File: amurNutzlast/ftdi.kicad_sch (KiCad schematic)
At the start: 23 parts, among them U4 FT2232HL, U5 93LCxxA, Y1 Crystal_GND24_Small

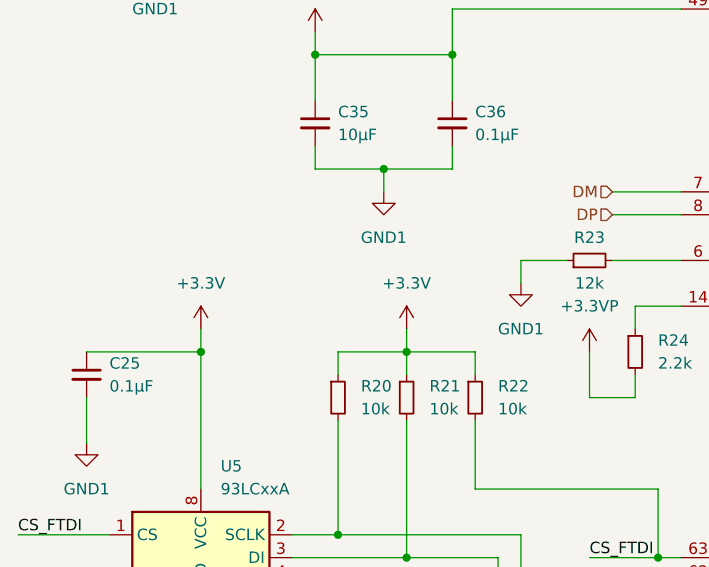
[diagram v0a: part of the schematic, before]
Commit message: ftdi layout finish
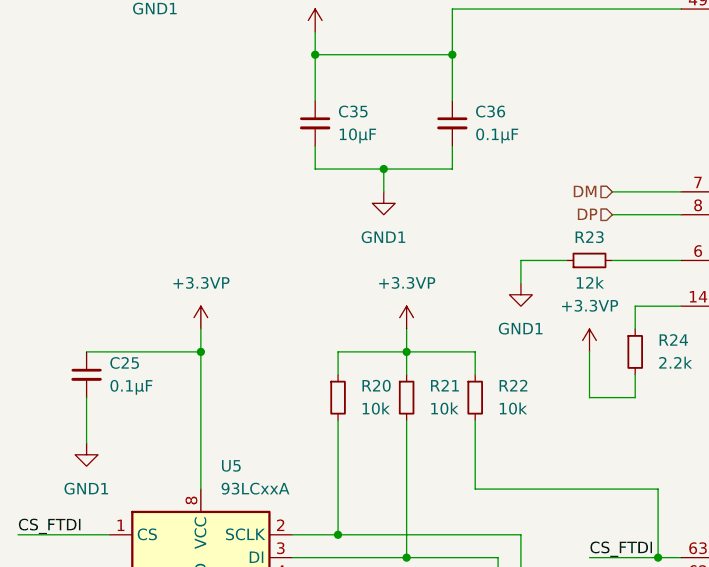
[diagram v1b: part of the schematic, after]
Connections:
- net +3.3V is gone; now on net +3.3VP: C25.1, R20.1, R21.1, R22.1, U5.8 (VCC)
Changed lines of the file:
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@@
     (effects (font (size 1.27 1.27)) (justify left))
   )
-  (symbol (lib_id "power:+3.3V") (at 76.2 114.3 0) (unit 1)
-    (in_bom yes) (on_board yes) (dnp no) (fields_autoplaced)
-    (property "Reference" "#PWR057" (at 76.2 118.11 0)
-      (effects (font (size 1.27 1.27)) hide)
-    )
-    (property "Value" "+3.3V" (at 76.2 109.22 0)
-      (effects (font (size 1.27 1.27)))
-    )
-    (property "Footprint" "" (at 76.2 114.3 0)
-      (effects (font (size 1.27 1.27)) hide)
-    )
-    (property "Datasheet" "" (at 76.2 114.3 0)
-      (effects (font (size 1.27 1.27)) hide)
-    )
-    (pin "1")
-    (instances
-      (project "amurNutzlast"
-        (path "/81bb76b1-eb1b-4eda-9d04-3f9c2ab6907c/baccd8b0-0f8a-4d7f-90a2-78ebcab7896d"
-          (reference "#PWR057") (unit 1)
+  (symbol (lib_id "power:+3.3VP") (at 53.34 114.3 0) (unit 1)
+    (in_bom yes) (on_board yes) (dnp no) (fields_autoplaced)
+    (property "Reference" "#PWR055" (at 57.15 115.57 0)
+      (effects (font (size 1.27 1.27)) hide)
+    )
+    (property "Value" "+3.3VP" (at 53.34 109.22 0)
+      (effects (font (size 1.27 1.27)))
+    )
+    (property "Footprint" "" (at 53.34 114.3 0)
+      (effects (font (size 1.27 1.27)) hide)
+    )
+    (property "Datasheet" "" (at 53.34 114.3 0)
+      (effects (font (size 1.27 1.27)) hide)
+    )
+    (pin "1")
+    (instances
+      (project "amurNutzlast"
+        (path "/81bb76b1-eb1b-4eda-9d04-3f9c2ab6907c/baccd8b0-0f8a-4d7f-90a2-78ebcab7896d"
+          (reference "#PWR055") (unit 1)
         )
       )
@@
     )
   )
-  (symbol (lib_id "power:+3.3V") (at 53.34 114.3 0) (unit 1)
-    (in_bom yes) (on_board yes) (dnp no) (fields_autoplaced)
-    (property "Reference" "#PWR055" (at 53.34 118.11 0)
-      (effects (font (size 1.27 1.27)) hide)
-    )
-    (property "Value" "+3.3V" (at 53.34 109.22 0)
-      (effects (font (size 1.27 1.27)))
-    )
-    (property "Footprint" "" (at 53.34 114.3 0)
-      (effects (font (size 1.27 1.27)) hide)
-    )
-    (property "Datasheet" "" (at 53.34 114.3 0)
-      (effects (font (size 1.27 1.27)) hide)
-    )
-    (pin "1")
-    (instances
-      (project "amurNutzlast"
-        (path "/81bb76b1-eb1b-4eda-9d04-3f9c2ab6907c/baccd8b0-0f8a-4d7f-90a2-78ebcab7896d"
-          (reference "#PWR055") (unit 1)
-        )
-      )
-    )
-  )
   (symbol (lib_id "Device:Crystal_GND24_Small") (at 88.9 157.48 270) (unit 1)
     (in_bom yes) (on_board yes) (dnp no) (fields_autoplaced)
@@
         )
       )
+    )
+  )
+  (symbol (lib_id "power:+3.3VP") (at 76.2 114.3 0) (unit 1)
+    (in_bom yes) (on_board yes) (dnp no) (fields_autoplaced)
+    (property "Reference" "#PWR057" (at 80.01 115.57 0)
+      (effects (font (size 1.27 1.27)) hide)
+    )
+    (property "Value" "+3.3VP" (at 76.2 109.22 0)
+      (effects (font (size 1.27 1.27)))
+    )
+    (property "Footprint" "" (at 76.2 114.3 0)
+      (effects (font (size 1.27 1.27)) hide)
+    )
+    (property "Datasheet" "" (at 76.2 114.3 0)
+      (effects (font (size 1.27 1.27)) hide)
+    )
+    (pin "1")
+    (instances
+      (project "amurNutzlast"
+        (path "/81bb76b1-eb1b-4eda-9d04-3f9c2ab6907c/baccd8b0-0f8a-4d7f-90a2-78ebcab7896d"
+          (reference "#PWR057") (unit 1)
+        )
+      )
